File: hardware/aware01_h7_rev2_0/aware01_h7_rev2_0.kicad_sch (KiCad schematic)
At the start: 14 parts, among them J2 Conn_02x07_Odd_Even, SW1 SW_Push, U2 STM32H7A3RITx, Y2 WE-XTAL 24.0MHz 50ppm

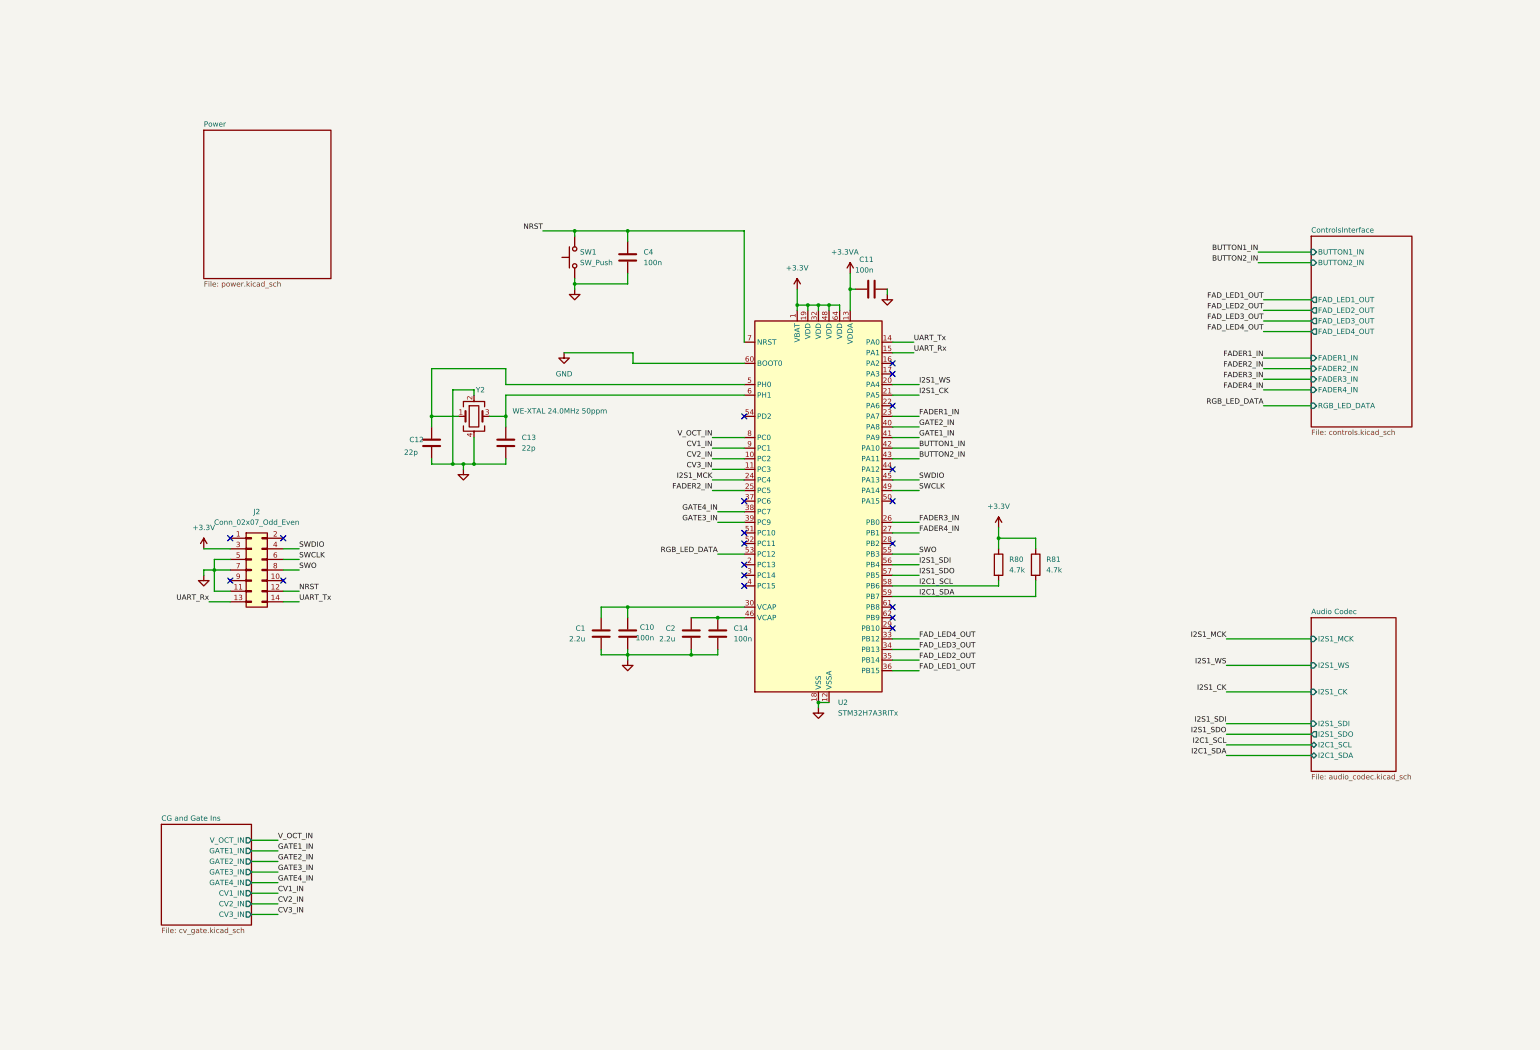
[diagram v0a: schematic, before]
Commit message: schematic formatting
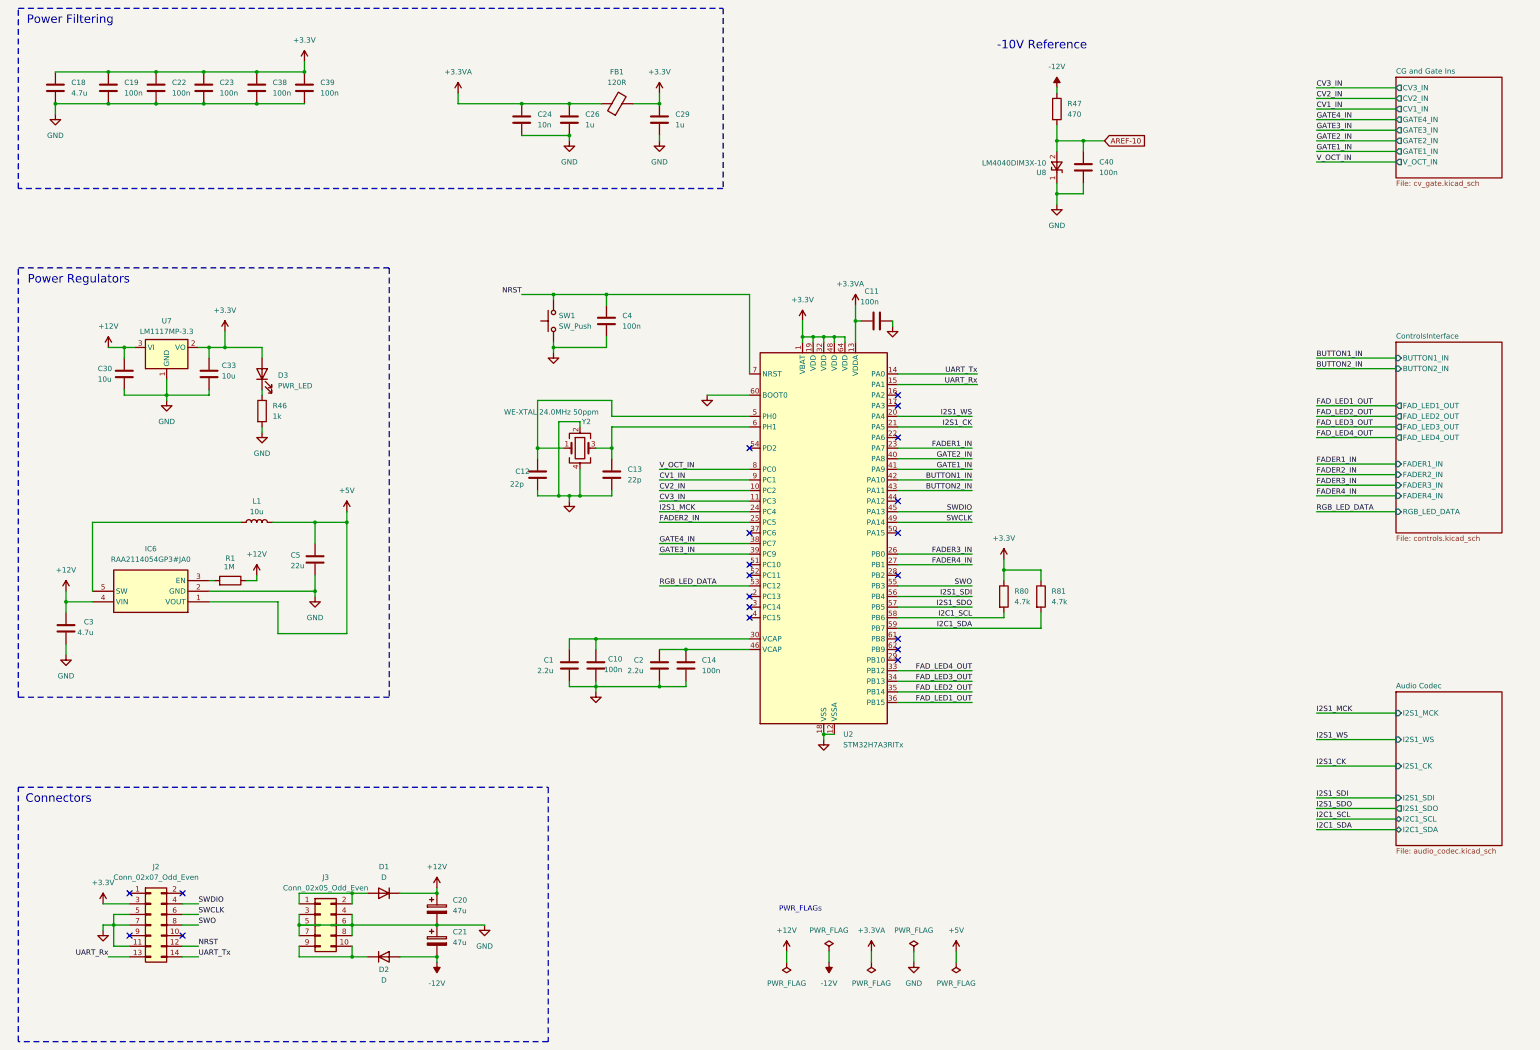
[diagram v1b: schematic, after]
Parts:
- added C18, C3: 4.7u, Capacitor_SMD:C_0603_1608Metric, symbol Device:C
- added C19, C22, C23, C38, C39, C40: 100n, Capacitor_SMD:C_0603_1608Metric, symbol Device:C
- added C20, C21: 47u, Capacitor_SMD:CP_Elec_6.3x5.9, symbol Device:C_Polarized
- added C24: 10n, Capacitor_SMD:C_0603_1608Metric, symbol Device:C
- added C26, C29: 1u, Capacitor_SMD:C_0603_1608Metric, symbol Device:C
- added C30, C33: 10u, Capacitor_SMD:C_0603_1608Metric, symbol Device:C
- added C5: 22u, Capacitor_SMD:C_0805_2012Metric_Pad1.18x1.45mm_HandSolder, symbol Device:C
- added D1, D2: D, Diode_SMD:D_0805_2012Metric, symbol Device:D
- added D3: PWR_LED, LED_SMD:LED_0603_1608Metric_Pad1.05x0.95mm_HandSolder, symbol Device:LED
- added FB1: 120R, Inductor_SMD:L_0805_2012Metric_Pad1.05x1.20mm_HandSolder, symbol Device:FerriteBead
- added IC6: RAA2114054GP3#JA0, Eurorack:RAA2114054GP3#JA0, symbol eurorack_components:RAA2114054GP3#JA0
- added J3: Conn_02x05_Odd_Even, Eurorack:PinHeader_2x05_P2.54mm_BHR-10-VUA, symbol Connector_Generic:Conn_02x05_Odd_Even
- added L1: 10u, Eurorack:74438335100, symbol Device:L
- added R1: 1M, Resistor_SMD:R_0603_1608Metric_Pad0.98x0.95mm_HandSolder, symbol Device:R
- added R46: 1k, Resistor_SMD:R_0603_1608Metric_Pad0.98x0.95mm_HandSolder, symbol Device:R
- added R47: 470, Resistor_SMD:R_0603_1608Metric_Pad0.98x0.95mm_HandSolder, symbol Device:R
- added U7: LM1117MP-3.3, Package_TO_SOT_SMD:SOT-223-3_TabPin2, symbol Regulator_Linear:LM1117MP-3.3
- added U8: LM4040DIM3X-10, Package_TO_SOT_SMD:SOT-23, symbol Reference_Voltage:LM4040DBZ-10
- R80, R81: Manufacturer_Name (none) -> YAGEO; Manufacturer_Part_Number (none) -> RC0603FR-134K7L; Mouser Part Number (none) -> 603-RC0603FR-134K7L
- U2: Manufacturer_Name (none) -> STMicroelectronics; Manufacturer_Part_Number (none) -> STM32H7A3RIT6TR; Mouser Part Number (none) -> 511-STM32H7A3RIT6TR
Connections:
- net +3.3V: now also C18.1, C19.1, C22.1, C23.1, C29.1, C33.1, C38.1, C39.1, D3.2 (A), FB1.2, U7.2 (VO)
- net +3.3VA: now also C24.1, C26.1, FB1.1
- net GND: now also C18.2, C19.2, C20.2, C21.1, C22.2, C23.2, C24.2, C26.2, C29.2, C3.1, C30.2, C33.2, C38.2, C39.2, C40.2, C5.2, IC6.2 (GND), J3.3 (Pin_3), J3.4 (Pin_4), J3.5 (Pin_5), J3.6 (Pin_6), J3.7 (Pin_7), J3.8 (Pin_8), R46.2, U7.1 (GND), U8.1 (K)
- new net: IC6.3 (EN), R1.2
- new net: D3.1 (K), R46.1
- new net: IC6.5 (SW), L1.1
- new net: D2.1 (K), J3.10 (Pin_10), J3.9 (Pin_9)
- new net: D1.2 (A), J3.1 (Pin_1), J3.2 (Pin_2)
- new net +12V: C20.1, C3.2, C30.1, D1.1 (K), IC6.4 (VIN), R1.1, U7.3 (VI)
- new net +5V: C5.1, IC6.1 (VOUT), L1.2
- new net -12V: C21.2, D2.2 (A), R47.1
- new net AREF-10: C40.1, R47.2, U8.2 (A)
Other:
- removed sheet Power
- note added: "-10V Reference"
- note added: "Connectors"
- note added: "PWR_FLAGs"
- note added: "Power Filtering"
- note added: "Power Regulators"
- moved on the sheet: C1, C10, C11, C12, C13, C14, C2, C4, J2, R80, R81, SW1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

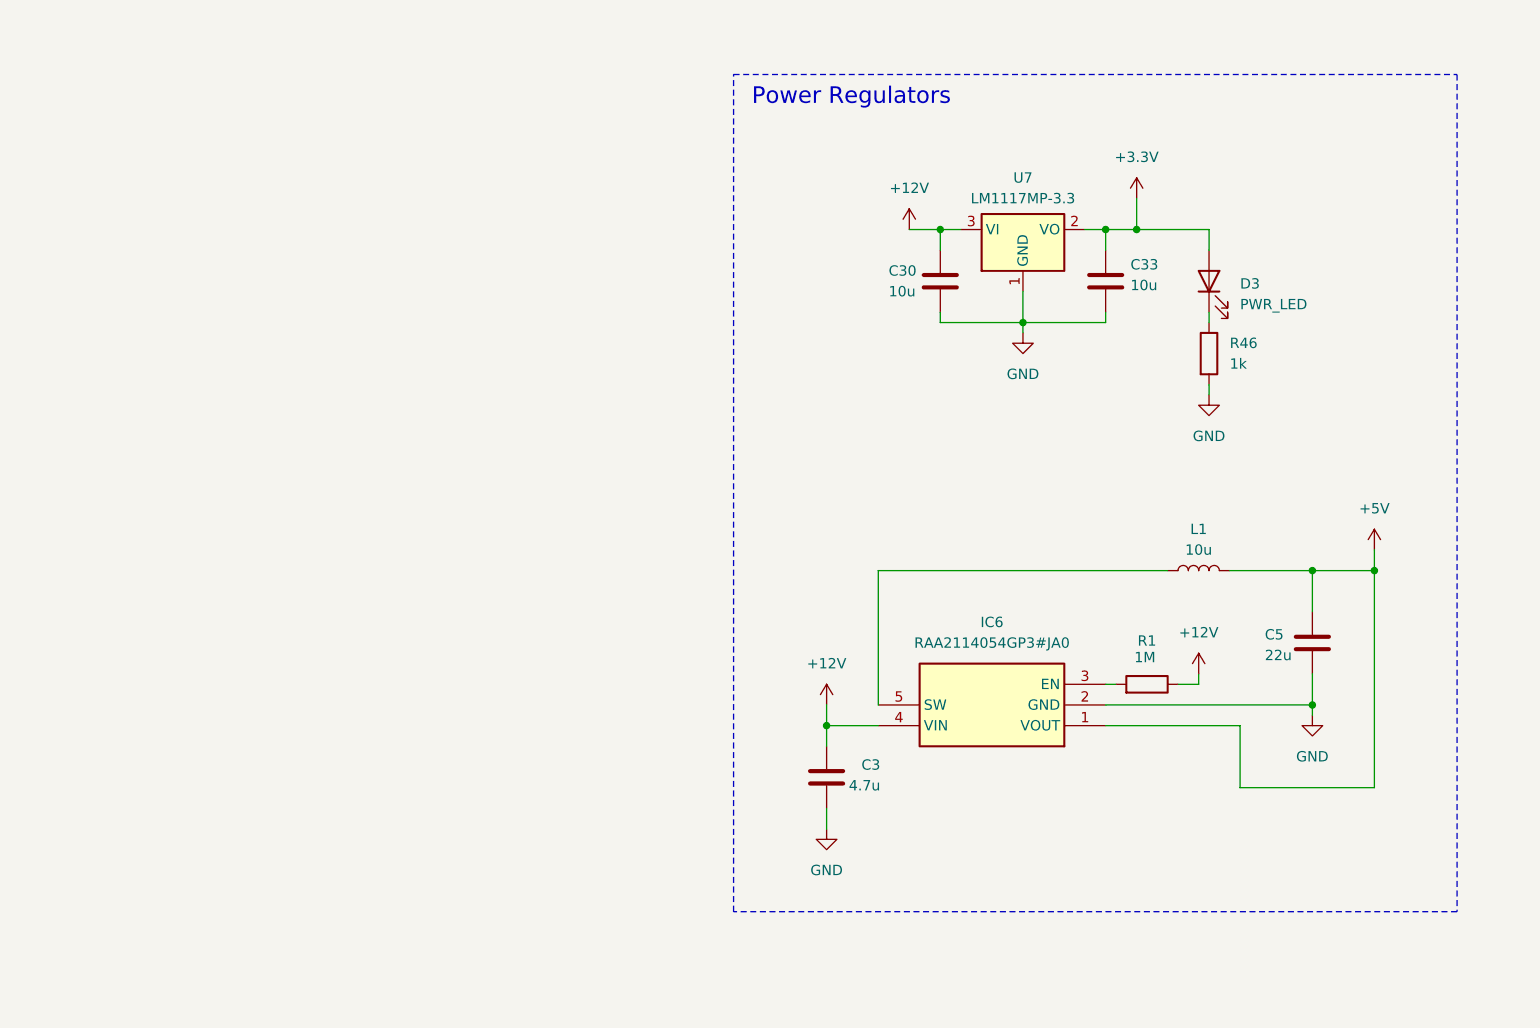
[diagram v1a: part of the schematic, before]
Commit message: update pcb with 5V buck converter
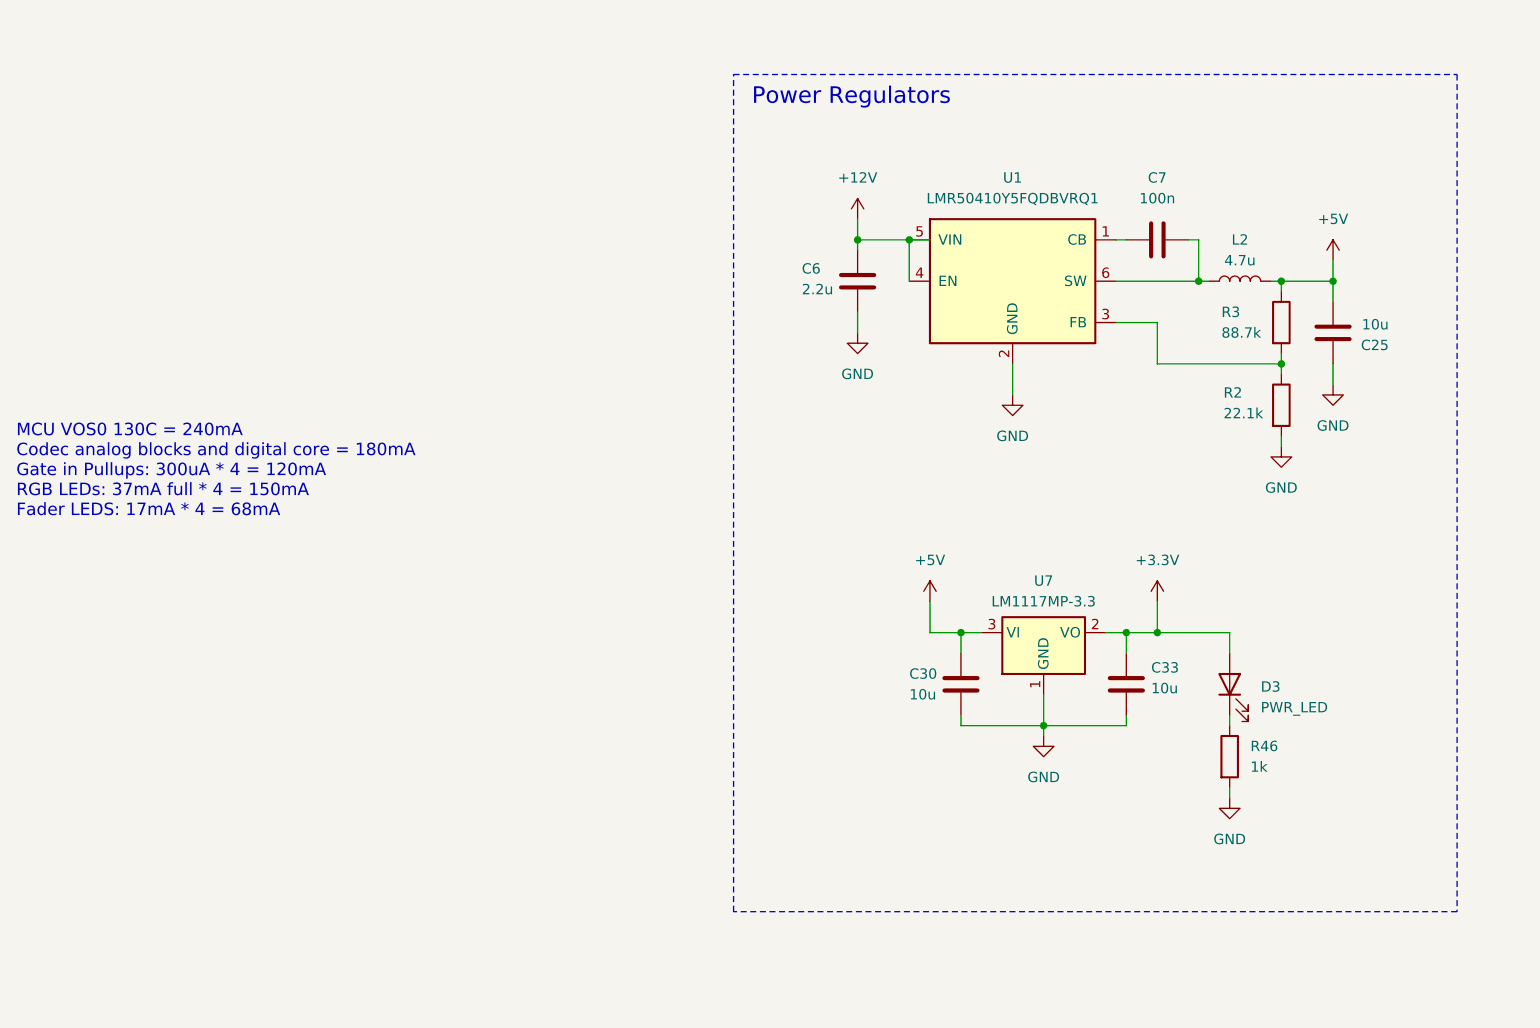
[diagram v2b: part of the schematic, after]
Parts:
- removed C3: 4.7u, Capacitor_SMD:C_0603_1608Metric, symbol Device:C
- removed C5: 22u, Capacitor_SMD:C_0805_2012Metric_Pad1.18x1.45mm_HandSolder, symbol Device:C
- removed IC6: RAA2114054GP3#JA0, Eurorack:RAA2114054GP3#JA0, symbol eurorack_components:RAA2114054GP3#JA0
- removed L1: 10u, Eurorack:74438335100, symbol Device:L
- removed R1: 1M, Resistor_SMD:R_0603_1608Metric_Pad0.98x0.95mm_HandSolder, symbol Device:R
- added C25: 10u, Capacitor_SMD:C_0603_1608Metric, symbol Device:C
- added C6: 2.2u, Capacitor_SMD:C_0603_1608Metric, symbol Device:C
- added C7: 100n, Capacitor_SMD:C_0603_1608Metric, symbol Device:C
- added L2: 4.7u, Eurorack:SRR5228A, symbol Device:L
- added R2: 22.1k, Resistor_SMD:R_0603_1608Metric_Pad0.98x0.95mm_HandSolder, symbol Device:R
- added R3: 88.7k, Resistor_SMD:R_0603_1608Metric_Pad0.98x0.95mm_HandSolder, symbol Device:R
- added U1: LMR50410Y5FQDBVRQ1, Package_TO_SOT_SMD:SOT-23-6, symbol Regulator_Switching:LMR50410
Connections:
- net +12V: now also C6.1, U1.4 (EN), U1.5 (VIN); no longer C30.1, U7.3 (VI)
- net +5V: now also C30.1, U7.3 (VI), C25.2, L2.2, R3.1
- net GND: now also C25.1, C6.2, R2.2, U1.2 (GND)
- new net: C7.1, L2.1, U1.6 (SW)
- new net: C7.2, U1.1 (CB)
- new net: R2.1, R3.2, U1.3 (FB)
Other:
- note added: "MCU VOS0 130C = 240mA Codec analog blocks and digital core = 180mA Gate in Pullups: 300uA * 4 = 120mA RGB LEDs: 37mA full * 4 = 150mA Fader LEDS: 17mA * 4 = 68mA"
- moved on the sheet: C30, C33, D3, R46, U7
